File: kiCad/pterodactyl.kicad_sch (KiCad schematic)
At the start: 155 parts, among them J0 Conn_01x03, SW0 MX, SW1 MX, SW10 MX, SW11 MX, SW12 MX, SW13 MX, SW14 MX, SW15 MX, SW16 MX, SW17 MX, SW18 MX, SW19 MX, SW2 MX, SW20 MX, SW21 MX, SW22 MX, SW23 MX, SW24 MX, SW25 MX, SW26 MX, SW27 MX, SW28 MX, SW29 MX, SW3 MX, SW30 MX, SW31 MX, SW32 MX, SW33 MX, SW34 MX, SW35 MX, SW36 MX, SW37 MX, SW38 MX, SW39 MX, SW4 MX, SW40 MX, SW41 MX, SW42 MX, SW43 MX, SW44 MX, SW45 MX, SW46 MX, SW47 MX, SW48 MX, SW49 MX, SW5 MX, SW50 MX, SW51 MX, SW52 MX, SW53 MX, SW54 MX, SW55 MX, SW56 MX, SW57 MX, SW58 MX, SW59 MX, SW6 RotaryEncoder_Switch, SW60 MX, SW61 MX, SW62 MX, SW63 MX, SW64 MX, SW65 MX, SW66 MX, SW67 MX, SW68 MX, SW69 MX, SW7 MX, SW70 MX, SW71 MX, SW72 MX, SW73 MX, SW74 MX, SW75 MX, SW76 MX, SW8 MX, SW9 MX, U0 Elite-C

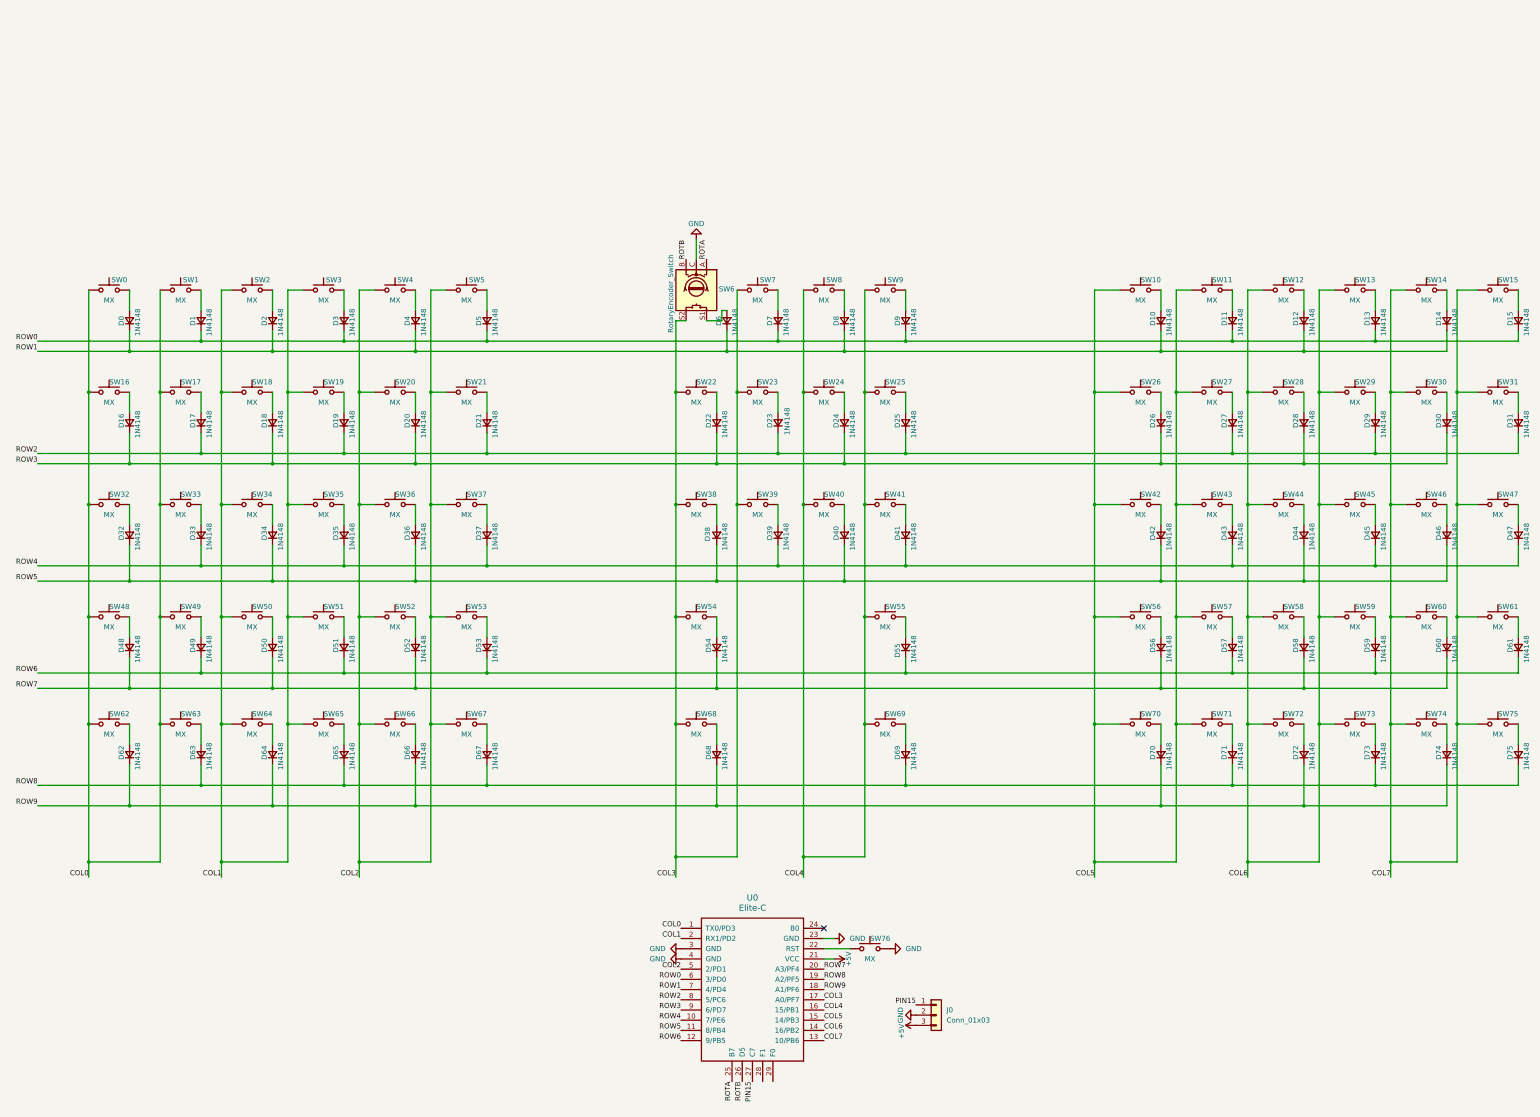
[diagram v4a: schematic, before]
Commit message: add most of routing
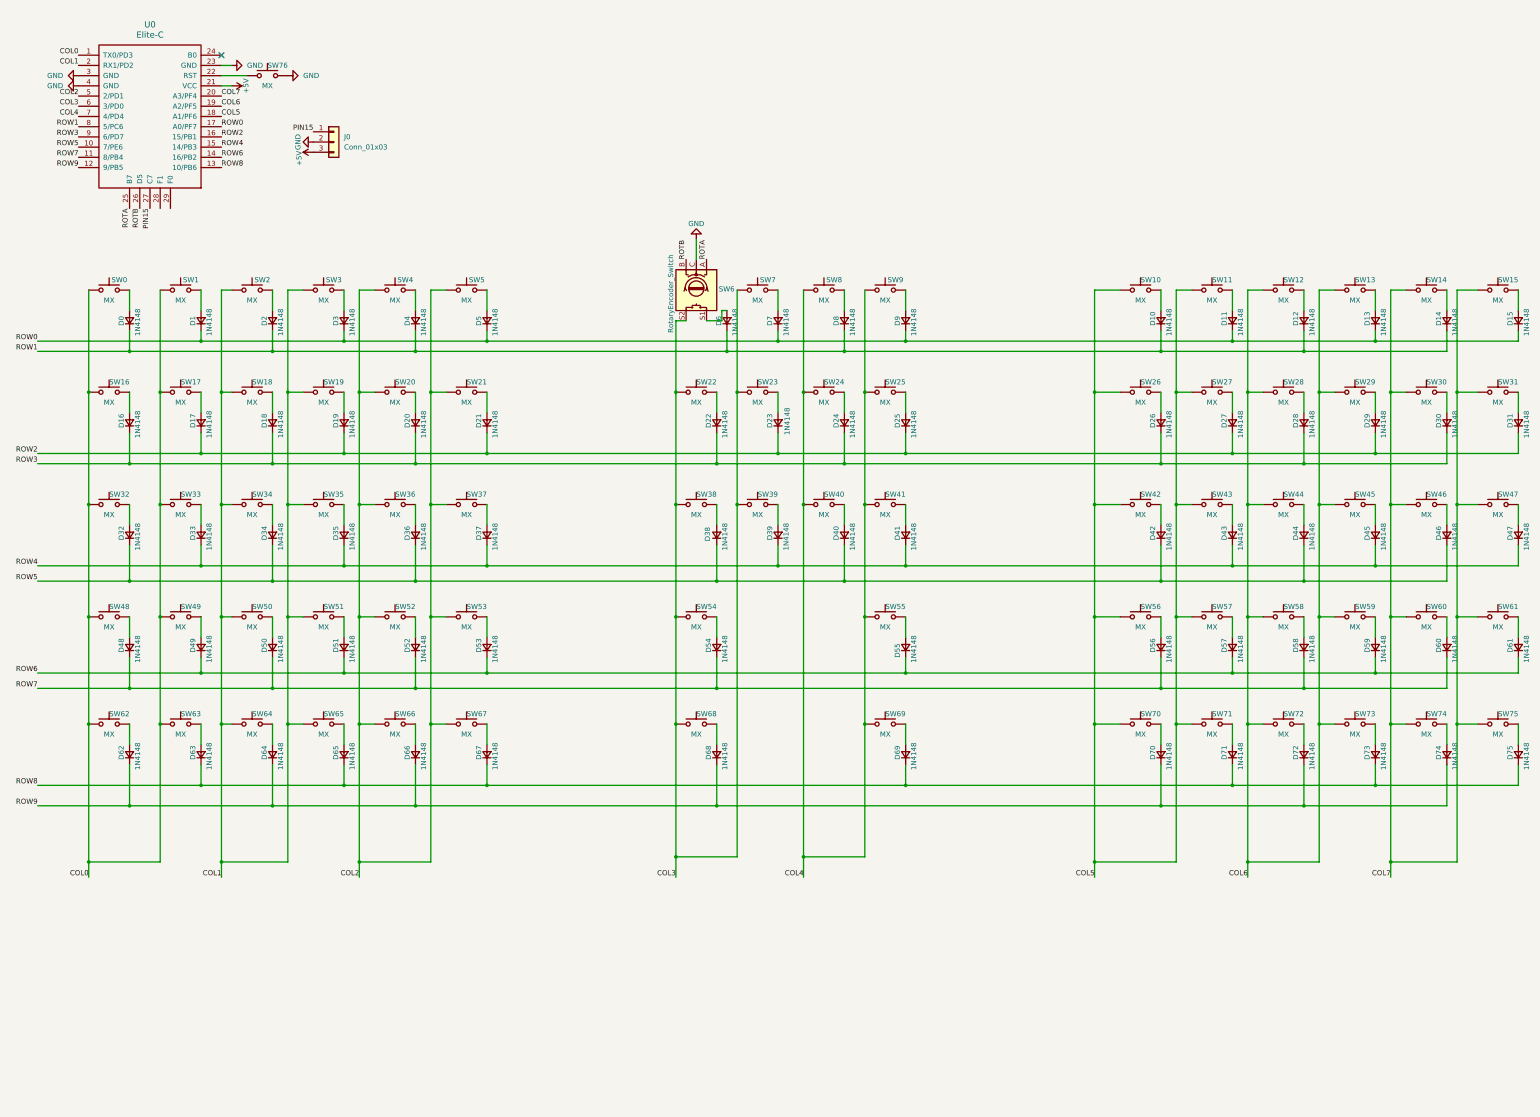
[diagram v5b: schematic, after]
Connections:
- net COL3: now also U0.6 (3/PD0); no longer U0.17 (A0/PF7)
- net COL4: now also U0.7 (4/PD4); no longer U0.16 (15/PB1)
- net COL5: now also U0.18 (A1/PF6); no longer U0.15 (14/PB3)
- net COL6: now also U0.19 (A2/PF5); no longer U0.14 (16/PB2)
- net COL7: now also U0.20 (A3/PF4); no longer U0.13 (10/PB6)
- net ROW0: now also U0.17 (A0/PF7); no longer U0.6 (3/PD0)
- net ROW1: now also U0.8 (5/PC6); no longer U0.7 (4/PD4)
- net ROW2: now also U0.16 (15/PB1); no longer U0.8 (5/PC6)
- net ROW4: now also U0.15 (14/PB3); no longer U0.10 (7/PE6)
- net ROW5: now also U0.10 (7/PE6); no longer U0.11 (8/PB4)
- net ROW6: now also U0.14 (16/PB2); no longer U0.12 (9/PB5)
- net ROW7: now also U0.11 (8/PB4); no longer U0.20 (A3/PF4)
- net ROW8: now also U0.13 (10/PB6); no longer U0.19 (A2/PF5)
- net ROW9: now also U0.12 (9/PB5); no longer U0.18 (A1/PF6)
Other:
- moved on the sheet: J0, SW76, U0
